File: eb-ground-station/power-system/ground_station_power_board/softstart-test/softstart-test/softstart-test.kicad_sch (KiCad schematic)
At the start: 10 parts, among them Q1 2n3904, Q2 IRF9530

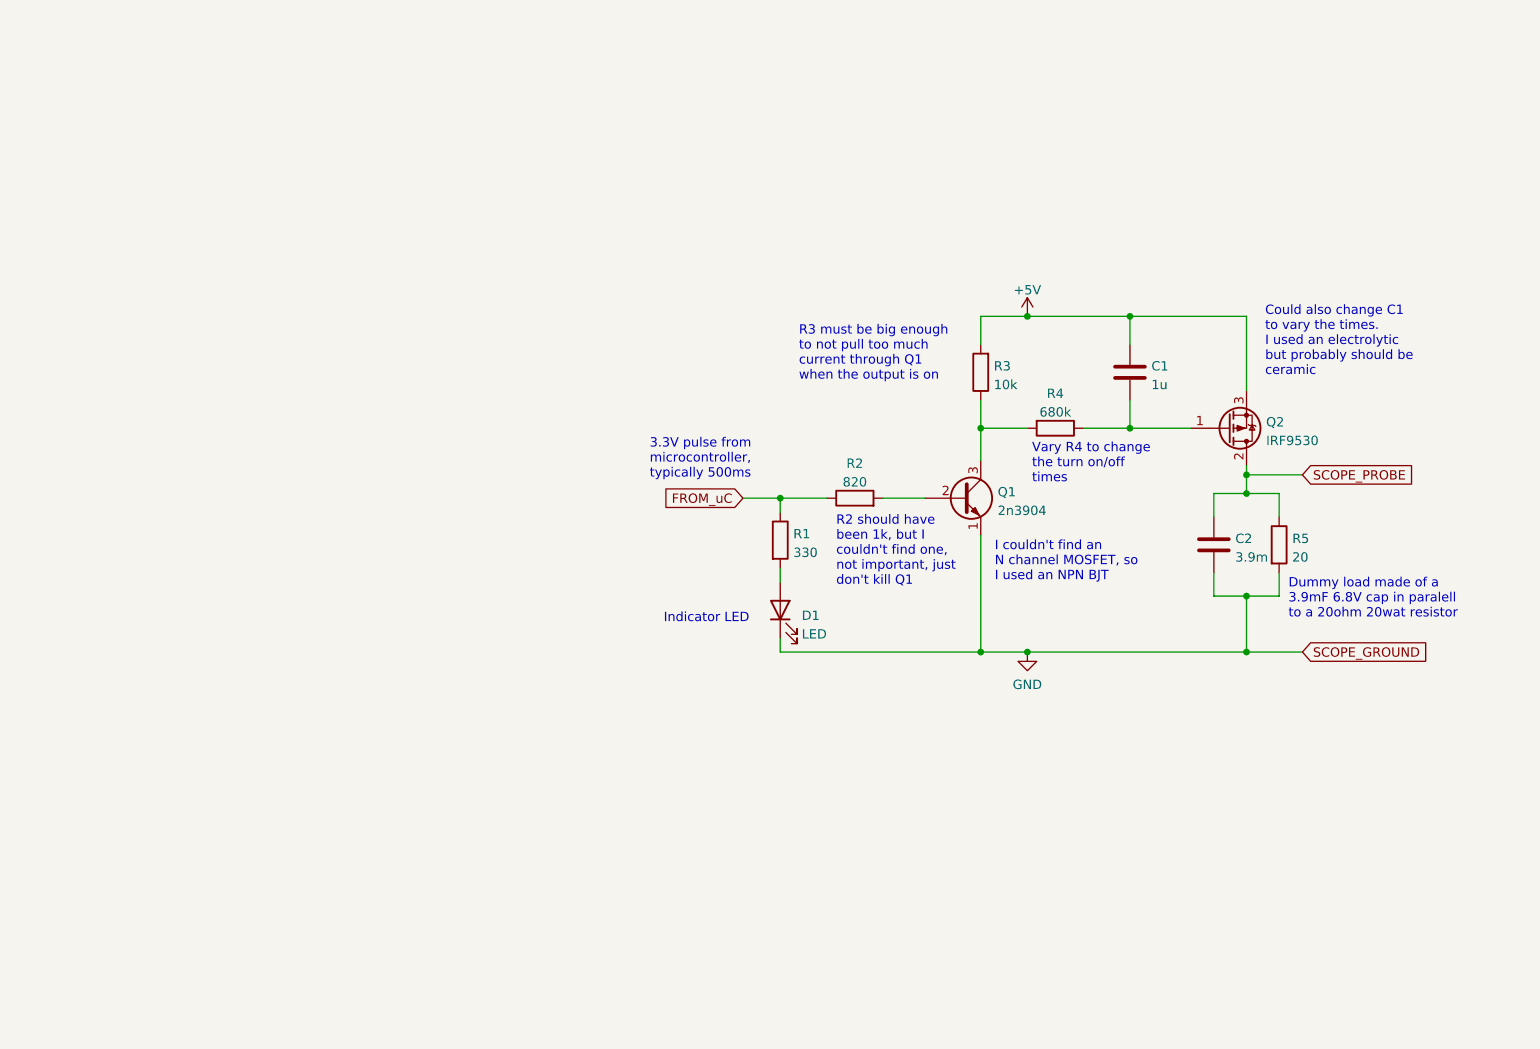
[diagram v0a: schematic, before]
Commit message: New power board schematic almost done
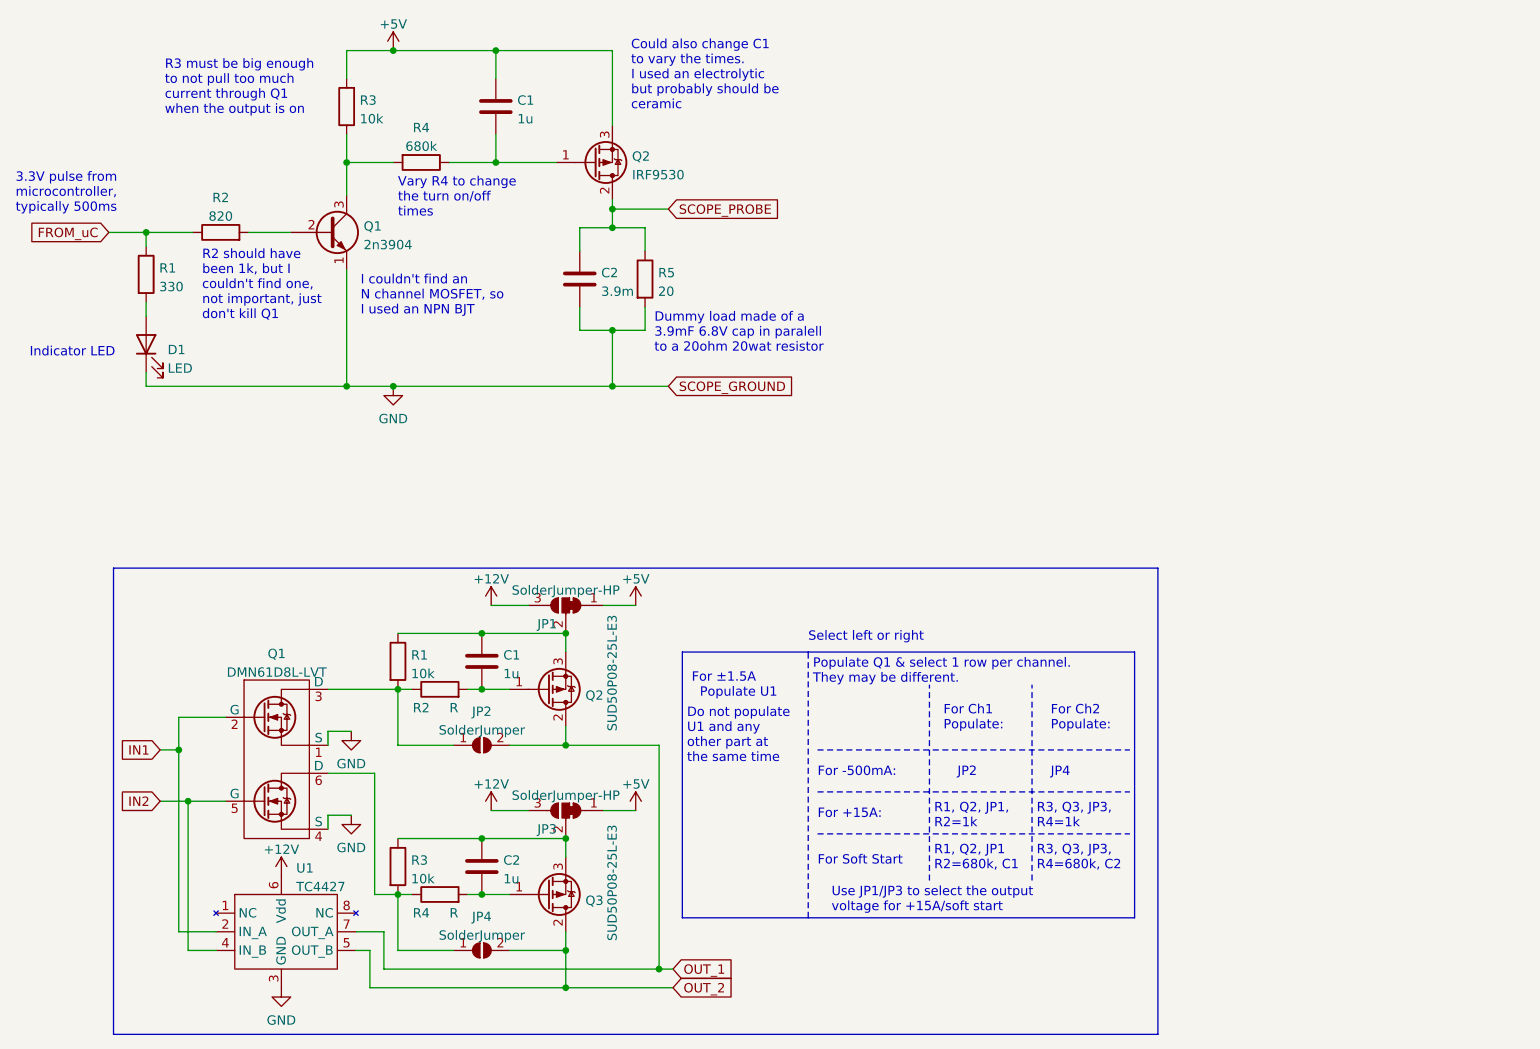
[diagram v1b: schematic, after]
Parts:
- added C1, C2: 1u, symbol Device:C
- added JP1, JP3: SolderJumper-HP, symbol Jumper:SolderJumper_3_Bridged12
- added JP2, JP4: SolderJumper, symbol Jumper:SolderJumper_2_Open
- added Q1: DMN61D8L-LVT, symbol OreSat-q-mosfet-DMN61D8L-LVT:DMN61D8L-LVT
- added Q2, Q3: SUD50P08-25L-E3, symbol Device:Q_PMOS_GDS
- added R1, R3: 10k, symbol Device:R
- added R2, R4: R, symbol Device:R
- added U1: TC4427, symbol OreSat-q-mosfet-driver-TC4427:TC4427
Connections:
- net +5V: now also JP1.1 (A), JP3.1 (A)
- net GND: now also Q1.1 (S), Q1.4 (S), U1.3 (GND)
- new net: JP4.1 (A), Q1.6 (D), R3.2, R4.1
- new net: C2.1, JP3.2 (C), Q3.3 (S), R3.1
- new net: C2.2, Q3.1 (G), R4.2
- new net: JP2.1 (A), Q1.3 (D), R1.2, R2.1
- new net: C1.1, JP1.2 (C), Q2.3 (S), R1.1
- new net: C1.2, Q2.1 (G), R2.2
- new net +12V: JP1.3 (B), JP3.3 (B), U1.6 (Vdd)
- new net IN1: Q1.2 (G), U1.2 (IN_A)
- new net IN2: Q1.5 (G), U1.4 (IN_B)
- new net OUT_1: JP2.2 (B), Q2.2 (D), U1.7 (OUT_A)
- new net OUT_2: JP4.2 (B), Q3.2 (D), U1.5 (OUT_B)
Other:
- note added: "Do not populate U1 and any other part at the same time"
- note added: "For +15A:"
- note added: "For -500mA:"
- note added: "For Ch1 Populate:"
- note added: "For Ch2 Populate:"
- note added: "For Soft Start"
- note added: "For ±1.5A Populate U1"
- note added: "JP2"
- note added: "JP4"
- note added: "Populate Q1 & select 1 row per channel. They may be different."
- note added: "R1, Q2, JP1 R2=680k, C1"
- note added: "R1, Q2, JP1, R2=1k"
- note added: "R3, Q3, JP3, R4=1k"
- note added: "R3, Q3, JP3, R4=680k, C2"
- note added: "Select left or right"
- note added: "Use JP1/JP3 to select the output voltage for +15A/soft start"
- moved on the sheet: C1, C2, D1, Q1, Q2, R1, R2, R3, R4, R5
